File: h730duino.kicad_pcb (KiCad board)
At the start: 4 copper layers, 101.6 x 53.3 mm, 115 parts, among them J1 USB_C_Receptacle_USB2.0, J2 USB_B_Micro, J3 L834-1G1T-91, J4 105162-0001, J5 Conn_ARM_JTAG_SWD_10, J6 Conn_ARM_JTAG_SWD_10, J7 Conn_02x03_Odd_Even, P1 Digital, P10 CONN_01X01, P11 CONN_01X01, P13 CONN_01X01, P2 Power, P3 Analog, P4 Analog, P5 PWM, P6 PWM, P7 Communication, P8 CONN_01X01, SW1 RESET, U1 STM32H730ZBT6, U10 APS6404L-3SQN, U12 AP22814BW5, U2 W25Q32JVSS, U3 TPS62162DSG, U4 TPS62163DSG, U5 MAX40200AUK, U6 MAX40200AUK, U7 STM32F042F6Px, U8 MAX40200AUK, U9 LAN8742A, Y1 32.768K, Y2 8M, Y3 25M

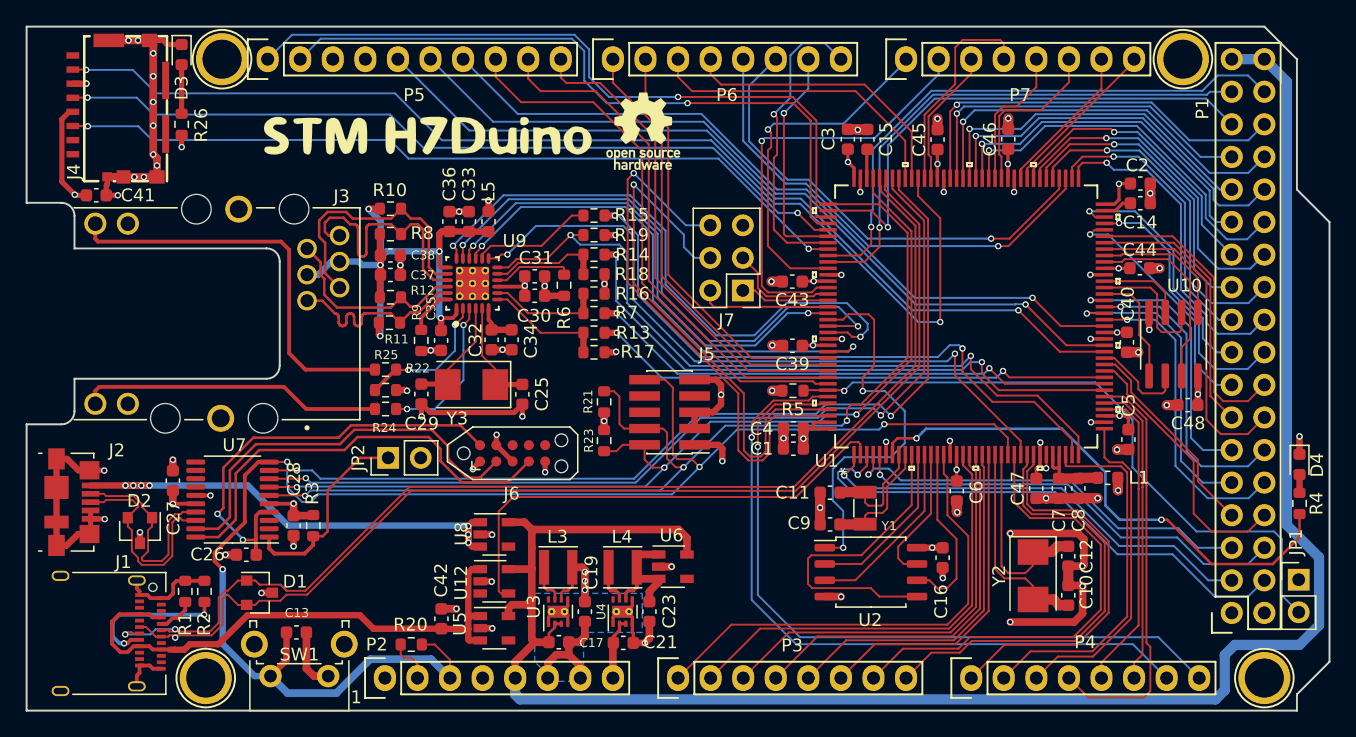
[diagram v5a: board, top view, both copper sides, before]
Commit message: Improve previous changes:
 - Add pullup resistors to uSD card slot
 - Reroute some signals for more space
 - Check impedance of QSPI/USB signals
 - Match length of uSD signals

Signed-off-by: Martin Ribelotta <martinribelotta@gmail.com>
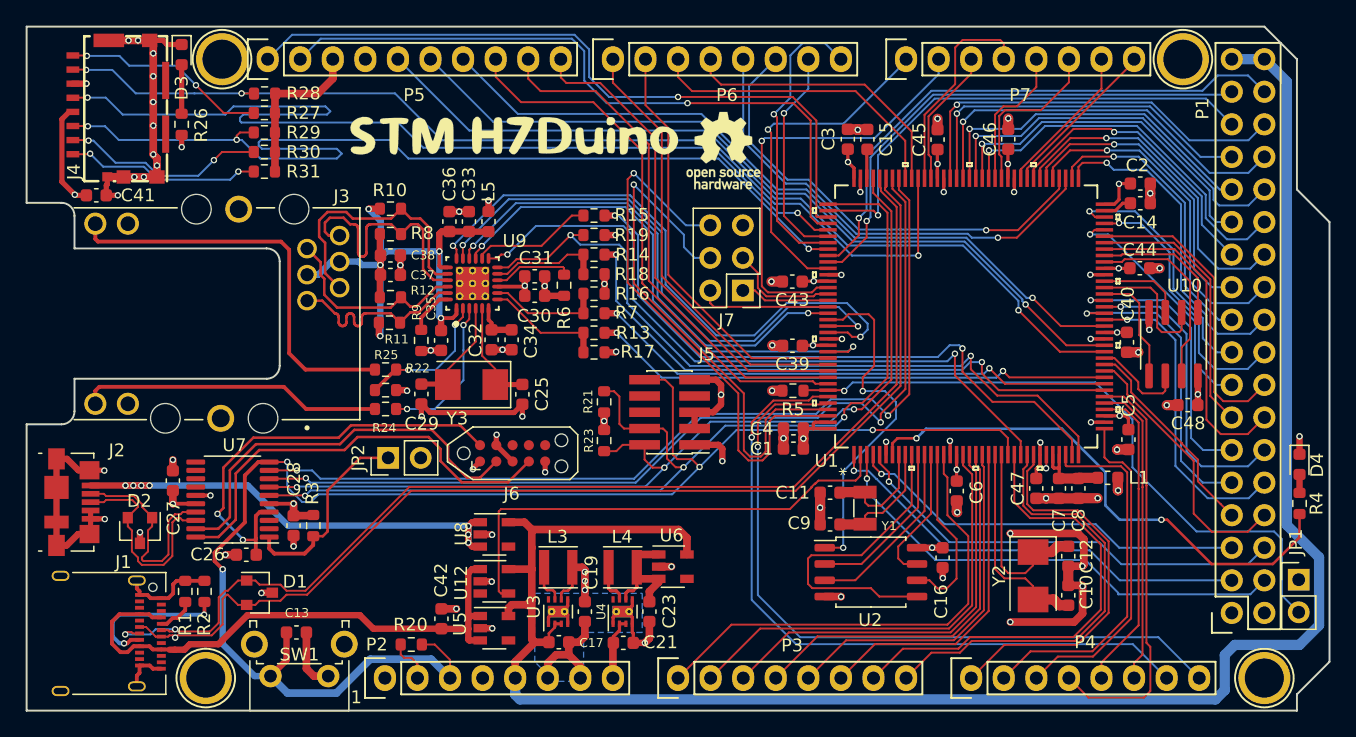
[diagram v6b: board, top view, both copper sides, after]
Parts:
- added R27: 10K, Resistor_SMD:R_0603_1608Metric, F.Cu at (121.9, 75.1)
- added R28: 10K, Resistor_SMD:R_0603_1608Metric, F.Cu at (121.9, 73.5)
- added R29: 10K, Resistor_SMD:R_0603_1608Metric, F.Cu at (121.9, 76.6)
- added R30: 10K, Resistor_SMD:R_0603_1608Metric, F.Cu at (121.9, 78.1)
- added R31: 10K, Resistor_SMD:R_0603_1608Metric, F.Cu at (121.9, 79.6)
- moved G1 6.74 mm to (141.4, 76.8)
- moved LOGO1 6.43 mm to (157.7, 78.0)
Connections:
- J4 pad 1: (no net) -> Net-(J4-Pad1)
- J4 pad 2: (no net) -> Net-(J4-Pad2)
- J4 pad 8: (no net) -> Net-(J4-Pad8)
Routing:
- net /SDMMC1_CMD: track 62.9 -> 79.0 mm, vias 2 -> 3
- net Net-(J4-Pad2): track 0.00 -> 16.0 mm, vias 0 -> 2
- net Net-(J4-Pad8): track 0.00 -> 16.0 mm, vias 0 -> 2
- net Net-(J4-Pad1): track 0.00 -> 15.2 mm, vias 0 -> 2
- net /SDMMC1_CK: track 63.2 -> 77.9 mm
- net +3V3: track 77.3 -> 89.9 mm
- net /SDMMC1_D0: track 87.7 -> 79.0 mm, vias 2 -> 3
- net /53(SS): track 41.7 -> 37.7 mm
- net /OCTOSPIM_P2_NCS: track 30.7 -> 27.3 mm
- net /24: track 40.7 -> 39.0 mm
- net /SWCLK: track 82.7 -> 81.2 mm
- net /50(MISO): track 32.8 -> 31.5 mm
- net /SWDIO: track 75.9 -> 74.6 mm
- net /52(SCK): track 35.5 -> 34.3 mm
- net /USB_OTG_HS_N: track 87.7 -> 86.5 mm
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
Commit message: Add new BOM to octopart
TODO: PSRAM is not recognized by Octopart but is available in LCSC

Signed-off-by: Martin Ribelotta <martinribelotta@gmail.com>
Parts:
- R24, R25: value 270R -> 220R
- U10: value APS6404L-3SQN -> LY68L6400SLI
- U12: value AP22814BW5 -> AP2161W
- U2: value W25Q32JVSS -> IS25LP032D-JBLE-TR

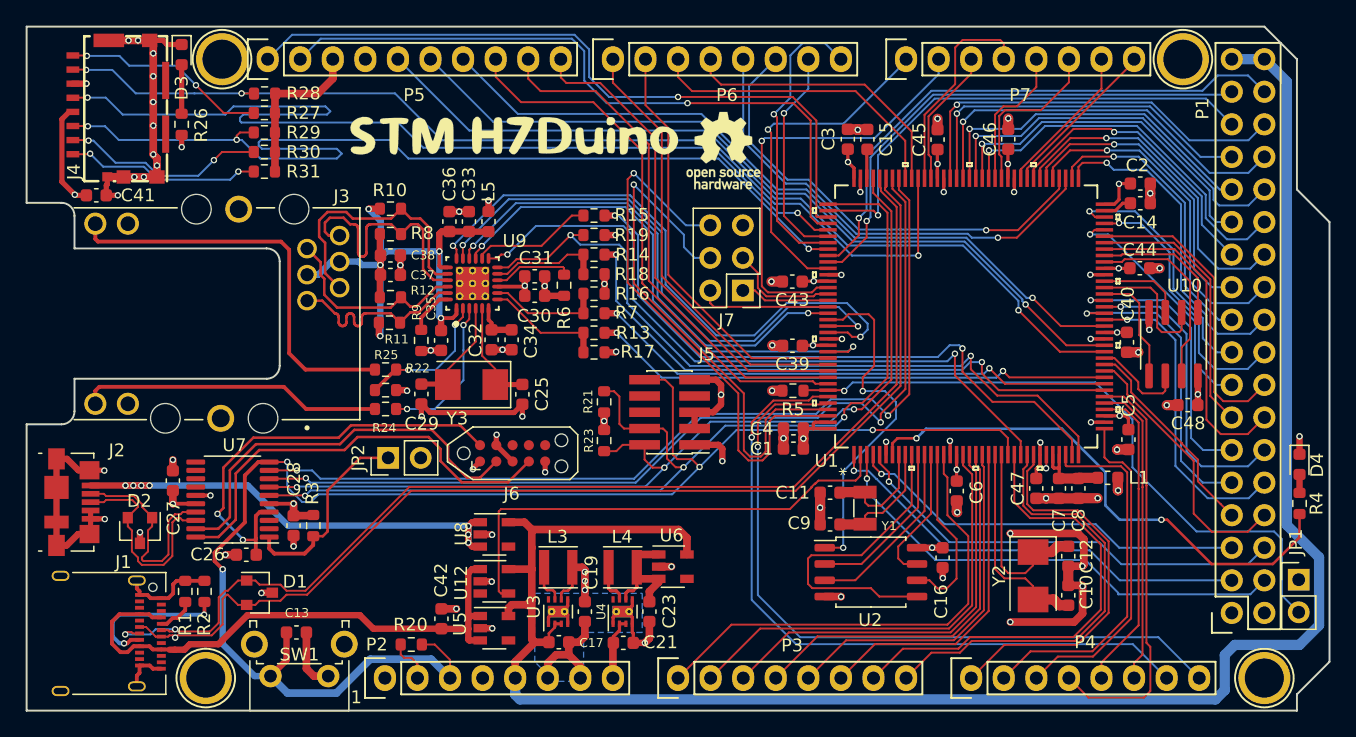
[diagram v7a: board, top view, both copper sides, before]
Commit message: Replace LAN8742 by KSZ8081RND/RNA
Signed-off-by: Martin Ribelotta <martinribelotta@gmail.com>
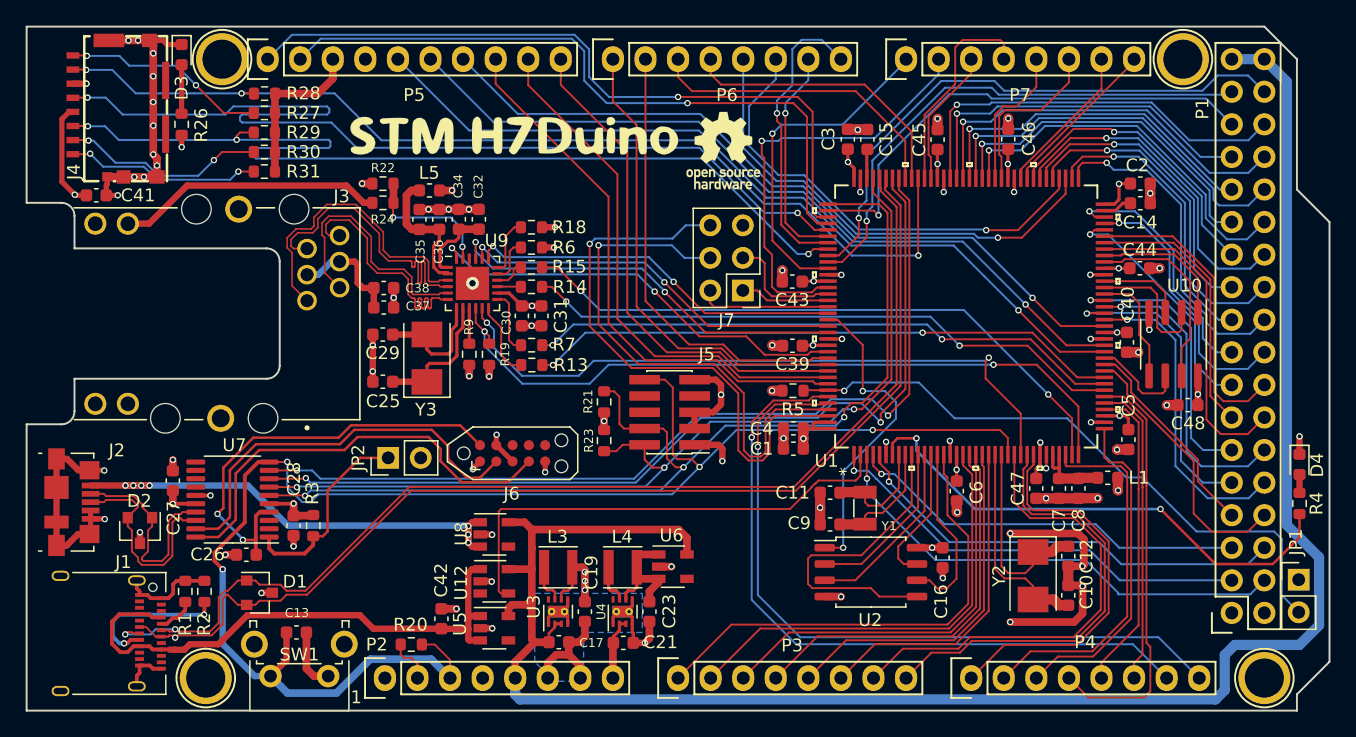
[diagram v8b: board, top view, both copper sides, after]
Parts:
- removed C33: 100n, Capacitor_SMD:C_0603_1608Metric
- removed R10, R11, R12, R8: 49.9R, Resistor_SMD:R_0603_1608Metric
- removed R16, R17: 10K, Resistor_SMD:R_0603_1608Metric
- removed R25: 220R, Resistor_SMD:R_0603_1608Metric
- C30, C36: value 10u -> 22u
- C32: value 470p -> 2.2u
- C37, C38: value 0.022u -> 100n
- P1: value Digital -> CONN_02x18
- P2: value Power -> CONN_01x08
- P3, P4: value Analog -> CONN_01x08
- P5: value PWM -> CONN_01x10
- P6: value PWM -> CONN_01x08
- P7: value Communication -> CONN_01x08
- R18: value 10K -> 1K5
- R9: value 12.1K 1% -> 6.49K 1%
- U9: value LAN8742A -> KSZ8081RNA; footprint footprints:Microchip-C04-143B-S4QFN-0-0-MFG -> Package_DFN_QFN:QFN-24-1EP_4x4mm_P0.5mm_EP2.6x2.6mm
- moved R22 16.1 mm to (131.2, 80.6)
- moved R24 16.1 mm to (131.2, 82.1)
- moved R19 12.4 mm to (139.4, 93.9), turned to 270 degrees
- moved C25 10.9 mm to (131.2, 96.0), turned to 0 degrees
- moved C34 10.3 mm to (137.1, 83.4), turned to 90 degrees
- moved C35 9.59 mm to (134.0, 83.4), turned to 90 degrees
- moved C32 9.45 mm to (138.6, 83.4), turned to 90 degrees
- moved R15 6.33 mm to (142.7, 87.1)
- moved R18 6.10 mm to (142.7, 84.0)
- moved C29 5.53 mm to (131.2, 92.3), turned to 0 degrees
- moved R14 5.49 mm to (142.7, 88.6)
- moved R7 5.46 mm to (142.8, 93.2)
- moved R13 5.46 mm to (142.8, 94.7)
- moved L5 5.20 mm to (134.8, 81.1), turned to 180 degrees
- moved Y3 4.04 mm to (134.6, 94.2), turned to 90 degrees
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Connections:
- C35 pad 1: Net-(C33-Pad1) -> Net-(C35-Pad1)
- C36 pad 1: Net-(C33-Pad1) -> Net-(C35-Pad1)
- C37 pad 1: Net-(C33-Pad1) -> GND
- C37 pad 2: GND -> Net-(C37-Pad2)
- C38 pad 1: Net-(C33-Pad1) -> Net-(C37-Pad2)
- J3 pad 11: Net-(C33-Pad1) -> Net-(C37-Pad2)
- J3 pad 13: GND -> (no net)
- J3 pad 14: Net-(J3-Pad14) -> (no net)
- J3 pad 15: GND -> Net-(J3-Pad15)
- J3 pad 16: Net-(J3-Pad16) -> +3V3
- J3 pad 4: /Ethernet/RX_P -> /Ethernet/RX_N
- J3 pad 5: Net-(C33-Pad1) -> Net-(C37-Pad2)
- J3 pad 6: /Ethernet/RX_N -> /Ethernet/RX_P
- L5 pad 2: Net-(C33-Pad1) -> Net-(C35-Pad1)
- R18 pad 2: Net-(R14-Pad1) -> Net-(R18-Pad2)
- R19 pad 1: +3V3 -> /ETH_MDIO
- R19 pad 2: /ETH_MDIO -> +3V3
- R22 pad 1: GND -> Net-(R22-Pad1)
- R22 pad 2: /Ethernet/LED2 -> +3V3
- R24 pad 1: /Ethernet/LED1 -> Net-(R22-Pad1)
- R24 pad 2: Net-(J3-Pad14) -> Net-(J3-Pad15)
- R7 pad 1: Net-(R16-Pad2) -> Net-(R7-Pad1)
- U9 pad 1: Net-(C33-Pad1) -> Net-(C32-Pad1)
- U9 pad 10: Net-(R6-Pad2) -> /ETH_MDIO
- U9 pad 11: Net-(R14-Pad1) -> /ETH_MDC
- U9 pad 12: /ETH_MDIO -> Net-(R13-Pad1)
- U9 pad 13: /ETH_MDC -> Net-(R7-Pad1)
- U9 pad 14: Net-(R15-Pad1) -> +3V3
- U9 pad 15: /~ETH_RST -> Net-(R14-Pad1)
- U9 pad 16: /ETH_TX_EN -> Net-(R15-Pad1)
- U9 pad 17: /ETH_TXD0 -> Net-(R6-Pad2)
- U9 pad 18: /ETH_TXD1 -> Net-(R18-Pad2)
- U9 pad 19: Net-(C33-Pad1) -> /ETH_TX_EN
- U9 pad 2: /Ethernet/LED2 -> Net-(C35-Pad1)
- U9 pad 20: /Ethernet/TX_N -> /ETH_TXD0
- U9 pad 21: /Ethernet/TX_P -> /ETH_TXD1
- U9 pad 22: /Ethernet/RX_N -> GND
- U9 pad 23: /Ethernet/RX_P -> Net-(R22-Pad1)
- U9 pad 24: Net-(R9-Pad1) -> /~ETH_RST
- U9 pad 3: /Ethernet/LED1 -> /Ethernet/RX_N
- U9 pad 4: Net-(C29-Pad2) -> /Ethernet/RX_P
- U9 pad 5: Net-(C25-Pad2) -> /Ethernet/TX_N
- U9 pad 6: Net-(C32-Pad1) -> /Ethernet/TX_P
- U9 pad 7: Net-(R13-Pad1) -> Net-(C29-Pad2)
- U9 pad 8: Net-(R16-Pad2) -> Net-(C25-Pad2)
- U9 pad 9: +3V3 -> Net-(R9-Pad1)
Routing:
- net Net-(C33-Pad1): track 43.7 -> 0.00 mm, vias 5 -> 0
- net Net-(J3-Pad16): track 32.0 -> 0.00 mm
- net Net-(J3-Pad14): track 23.7 -> 0.00 mm
- net Net-(J3-Pad15): track 0.00 -> 20.9 mm
- net /ETH_TXD1: track 47.7 -> 32.1 mm
- net /ETH_TXD0: track 44.8 -> 30.4 mm
- net /Ethernet/LED1: track 12.0 -> 0.00 mm, vias 2 -> 0
- net /Ethernet/LED2: track 11.1 -> 0.00 mm, vias 2 -> 0
- net Net-(R22-Pad1): track 0.00 -> 10.8 mm, vias 0 -> 2
- net Net-(C35-Pad1): track 0.00 -> 10.6 mm
- net /ETH_TX_EN: track 38.7 -> 29.4 mm
- net Net-(R16-Pad2): track 8.88 -> 0.00 mm
- net Net-(C37-Pad2): track 0.00 -> 8.84 mm
- net /Ethernet/RX_N: track 15.5 -> 23.8 mm
- net /Ethernet/RX_P: track 15.6 -> 23.8 mm
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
